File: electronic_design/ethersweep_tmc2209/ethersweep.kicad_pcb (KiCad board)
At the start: 2 copper layers, 79 x 38 mm, 101 parts, among them J1 AVR-ISP-6, J10 HR911105A, J11 Conn_01x04_Male, J2 Conn_01x02_Male, J3 Conn_01x04_Female, J4 Conn_01x02_Male, J5 Conn_01x02_Male, J6 Conn_01x07_Female, J7 Conn_01x07_Male, J8 AVR-ISP-6, J9 USB_B_Micro, SW1 SW_Push, U1 CP2102N-A01-GQFN28, U2 ATmega328-AU, U3 TMC2208-LA-T, U4 DD4012SA, U5 AS5600, U6 W5500, Y2 Crystal_25MHz, Y3 Crystal

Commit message: major commit for ethersweep 4 with STM32 MCU and USB C + fixes
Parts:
- removed C22: C100nF, Capacitor_SMD:C_0805_2012Metric
- removed G***: LOGO, ethernet_motor_driver:CODE Logo
- removed G***: LOGO, Logo:neumann_prototypen_tiny
- removed G***: LOGO, Logo:neumann_prototypen_small
- removed REF**: WEEE-Logo_4.2x6mm_SilkScreen, Symbol:WEEE-Logo_4.2x6mm_SilkScreen
- added C28: C100nF, Capacitor_SMD:C_0402_1005Metric, F.Cu at (252.1, 104.3)
- added C31: C10uF, Capacitor_SMD:C_0402_1005Metric, F.Cu at (212.3, 48.8)
- added J12: USB_C_Receptacle, Connector_USB:USB_C_Receptacle_XKB_U262-16XN-4BVC11, F.Cu at (199.6, 62.6)
- added U7: TMC2209-LA, KiCad:TMC2209-LA, F.Cu at (242.6, 31.8)
- added U8: STUSB4500QTR, Package_CSP:ST_WLCSP-25_Die444, F.Cu at (196.6, 55.6)
- C1, C12, C19, C20, C21, C23, C27, C29, C6: footprint Capacitor_SMD:C_0805_2012Metric -> Capacitor_SMD:C_0402_1005Metric
- C11: value C0.22uF -> C2.2-4.7uF ceramic; footprint Capacitor_SMD:C_0805_2012Metric -> Capacitor_SMD:C_1206_3216Metric
- C13, C35, C7: footprint Capacitor_SMD:C_0603_1608Metric -> Capacitor_SMD:C_0402_1005Metric
- C18: value C22nF -> C100nF; footprint Capacitor_SMD:C_0805_2012Metric -> Capacitor_SMD:C_0402_1005Metric
- C30: footprint Capacitor_SMD:C_0805_2012Metric -> Capacitor_SMD:C_0603_1608Metric
- C9: value C100nF -> C22nF 50V
- J4, J5: value Conn_01x02_Male -> Conn_01x03_Male; footprint Connector_JST:JST_EH_S2B-EH_1x02_P2.50mm_Horizontal -> Connector_JST:JST_EH_S3B-EH_1x03_P2.50mm_Horizontal
- R1, R14, R15, R16, R17, R2, R21, R22, R3: footprint Resistor_SMD:R_0603_1608Metric -> Resistor_SMD:R_0402_1005Metric
- R4, R5, R6, R7, R8: footprint Resistor_SMD:R_0805_2012Metric -> Resistor_SMD:R_0603_1608Metric
- U3: value TMC2208-LA-T -> STM32F103RBTx; footprint Package_DFN_QFN:TQFN-28-1EP_5x5mm_P0.5mm_EP3.25x3.25mm_ThermalVias -> Package_QFP:LQFP-64_10x10mm_P0.5mm
- moved C24 123.5 mm to (255.6, 107.8), turned to 0 degrees
- moved C14 116.4 mm to (275.8, 19.3)
- moved C25 114.3 mm to (256.2, 104.4)
- moved D2 114.3 mm to (302.3, 50.6), turned to 0 degrees
- moved R3 112.2 mm to (281.3, 41.6), turned to 0 degrees
- moved C19 111.9 mm to (314.9, 25.5)
- moved R24 109.1 mm to (298.6, 50.8), turned to 0 degrees
- moved R16 109.0 mm to (310.8, 23.1), turned to 0 degrees
- moved R17 108.3 mm to (311.3, 28.3)
- moved R14 102.0 mm to (285.3, 12.1), turned to 0 degrees
- moved C8 99.0 mm to (288.3, 32.3), turned to 0 degrees
- moved Y3 98.5 mm to (290.1, 25.8), turned to 0 degrees
- moved C10 94.3 mm to (291.2, 32.3), turned to 0 degrees
- moved C29 94.3 mm to (242.3, 41.8), turned to 0 degrees
- moved R15 90.5 mm to (290.6, 12.6), turned to 0 degrees
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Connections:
- C14 pad 1: +3.3VA -> +3V3
- C18 pad 1: Net-(C18-Pad1) -> +3.3VA
- C18 pad 2: Net-(C18-Pad2) -> GND
- C20 pad 1: Net-(C20-Pad1) -> +3.3VA
- C21 pad 1: Net-(C21-Pad1) -> +3.3VA
- C23 pad 2: GND -> Net-(C23-Pad2)
- C24 pad 1: +3.3VA -> GND
- C24 pad 2: GND -> Net-(C24-Pad2)
- C25 pad 1: +3.3VA -> Net-(C25-Pad1)
- C27 pad 1: rst -> +12V
- C27 pad 2: Net-(C27-Pad2) -> GND
- C29 pad 1: +3V3 -> +12V
- C9 pad 2: +12V -> Net-(C9-Pad2)
- J4 pad 2: ESTOP -> +3V3
- J5 pad 2: ENDSTOP -> +3V3
- J9 pad 1: Net-(C21-Pad1) -> Net-(C25-Pad1)
- R1 pad 2: ESTOP -> ENDSTOP
- R11 pad 1: Net-(R11-Pad1) -> GND
- R11 pad 2: GND -> Net-(R11-Pad2)
- R12 pad 1: Net-(R12-Pad1) -> GND
- R12 pad 2: GND -> Net-(R12-Pad2)
- R2 pad 2: ENDSTOP -> ESTOP
- RV1 pad 1: +3V3 -> GND
- RV1 pad 3: GND -> +3V3
- U1 pad 28: Net-(C27-Pad2) -> Net-(C28-Pad2)
- U1 pad 6: Net-(C20-Pad1) -> Net-(C24-Pad2)
- U1 pad 7: Net-(C21-Pad1) -> Net-(C25-Pad1)
- U1 pad 8: Net-(C21-Pad1) -> Net-(C25-Pad1)
- U2 pad 10: DIR -> unconnected-(U2-Pad10)
- U2 pad 11: STEP -> unconnected-(U2-Pad11)
- U2 pad 23: M1 -> unconnected-(U2-Pad23)
- U2 pad 24: M0 -> unconnected-(U2-Pad24)
- U2 pad 25: M2 -> unconnected-(U2-Pad25)
- U2 pad 26: FLT_STEPPER -> unconnected-(U2-Pad26)
- U2 pad 9: STEPPER_ENABLE -> unconnected-(U2-Pad9)
- U3 pad 1: Net-(J11-Pad4) -> unconnected-(U3-Pad1)
- U3 pad 10: M1 -> unconnected-(U3-Pad10)
- U3 pad 11: M2 -> unconnected-(U3-Pad11)
- U3 pad 12: FLT_STEPPER -> unconnected-(U3-Pad12)
- U3 pad 13: GND -> unconnected-(U3-Pad13)
- U3 pad 14: GND -> unconnected-(U3-Pad14)
- U3 pad 15: +3V3 -> unconnected-(U3-Pad15)
- U3 pad 16: STEP -> unconnected-(U3-Pad16)
- U3 pad 17: Net-(RV1-Pad2) -> unconnected-(U3-Pad17)
- U3 pad 18: GND -> unconnected-(U3-Pad18)
- U3 pad 19: DIR -> unconnected-(U3-Pad19)
- U3 pad 2: STEPPER_ENABLE -> unconnected-(U3-Pad2)
- U3 pad 20: GND -> unconnected-(U3-Pad20)
- U3 pad 21: Net-(J11-Pad1) -> unconnected-(U3-Pad21)
- U3 pad 22: +12V -> unconnected-(U3-Pad22)
- U3 pad 23: Net-(R11-Pad1) -> unconnected-(U3-Pad23)
- U3 pad 24: Net-(J11-Pad3) -> unconnected-(U3-Pad24)
- U3 pad 25: GND -> unconnected-(U3-Pad25)
- U3 pad 26: Net-(J11-Pad2) -> unconnected-(U3-Pad26)
- U3 pad 27: Net-(R12-Pad1) -> unconnected-(U3-Pad27)
- U3 pad 28: +12V -> unconnected-(U3-Pad28)
- U3 pad 29: GND -> unconnected-(U3-Pad29)
- U3 pad 3: GND -> unconnected-(U3-Pad3)
- U3 pad 4: Net-(C18-Pad1) -> unconnected-(U3-Pad4)
- U3 pad 5: Net-(C18-Pad2) -> unconnected-(U3-Pad5)
- U3 pad 6: Net-(C9-Pad1) -> unconnected-(U3-Pad6)
- U3 pad 7: GND -> unconnected-(U3-Pad7)
- U3 pad 8: Net-(C11-Pad1) -> unconnected-(U3-Pad8)
- U3 pad 9: M0 -> unconnected-(U3-Pad9)
- U6 pad 32: CS_ETHERNET -> GND
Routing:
- net +3V3: track 201.4 -> 117.3 mm, vias 10 -> 3
- net +12V: track 70.3 -> 0.00 mm, vias 6 -> 0
- net rst: track 62.0 -> 6.23 mm, vias 1 -> 0
- net STEPPER_ENABLE: track 40.4 -> 0.00 mm, vias 2 -> 0
- net FLT_STEPPER: track 38.2 -> 0.00 mm, vias 2 -> 0
- net GND: track 73.4 -> 36.4 mm, vias 226 -> 105
- net M2: track 36.2 -> 0.00 mm, vias 2 -> 0
- net SDA: track 115.7 -> 80.1 mm, vias 3 -> 0
- net M0: track 34.5 -> 0.00 mm, vias 2 -> 0
- net DIR: track 34.5 -> 0.00 mm, vias 2 -> 0
- net STEP: track 33.6 -> 0.00 mm, vias 2 -> 0
- net M1: track 32.9 -> 0.00 mm, vias 2 -> 0
- net uC_RX: track 31.2 -> 0.00 mm, vias 3 -> 0
- net SCL: track 109.9 -> 79.0 mm, vias 1 -> 0
- net ESTOP: track 68.9 -> 40.1 mm, vias 1 -> 0
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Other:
- board text added: "2023-01-10"
- board text added: "rev. 4.0.1"
- board text removed: "2022-10-05"
- board text removed: "3.3V"
- board text removed: "GND"
- board text removed: "RX"
- board text removed: "TX"
- board text removed: "rev. 3.0.5"

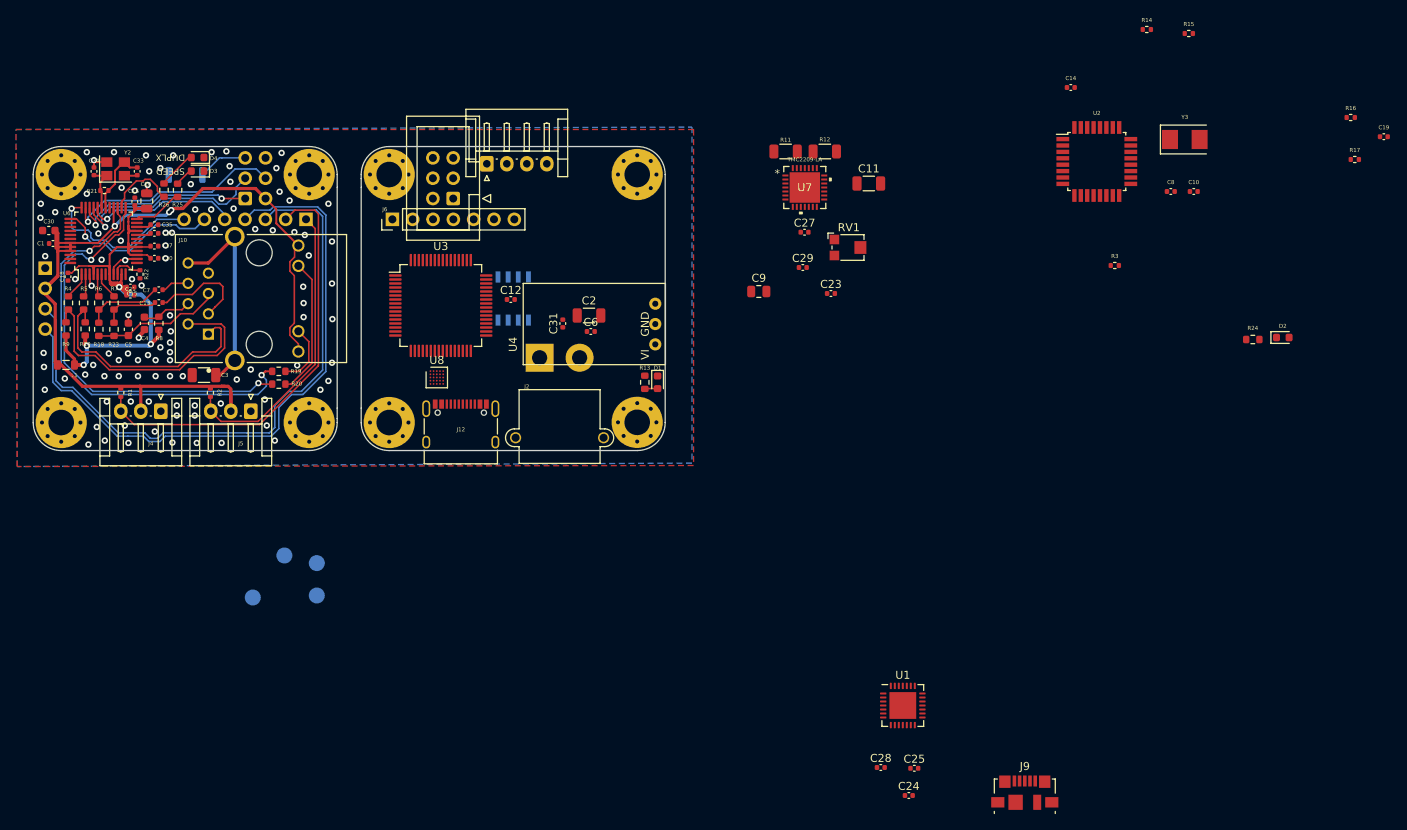
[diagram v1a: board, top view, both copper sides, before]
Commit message: cleanup, schmeatic design around USB connecotr, STM32 and reorganisation
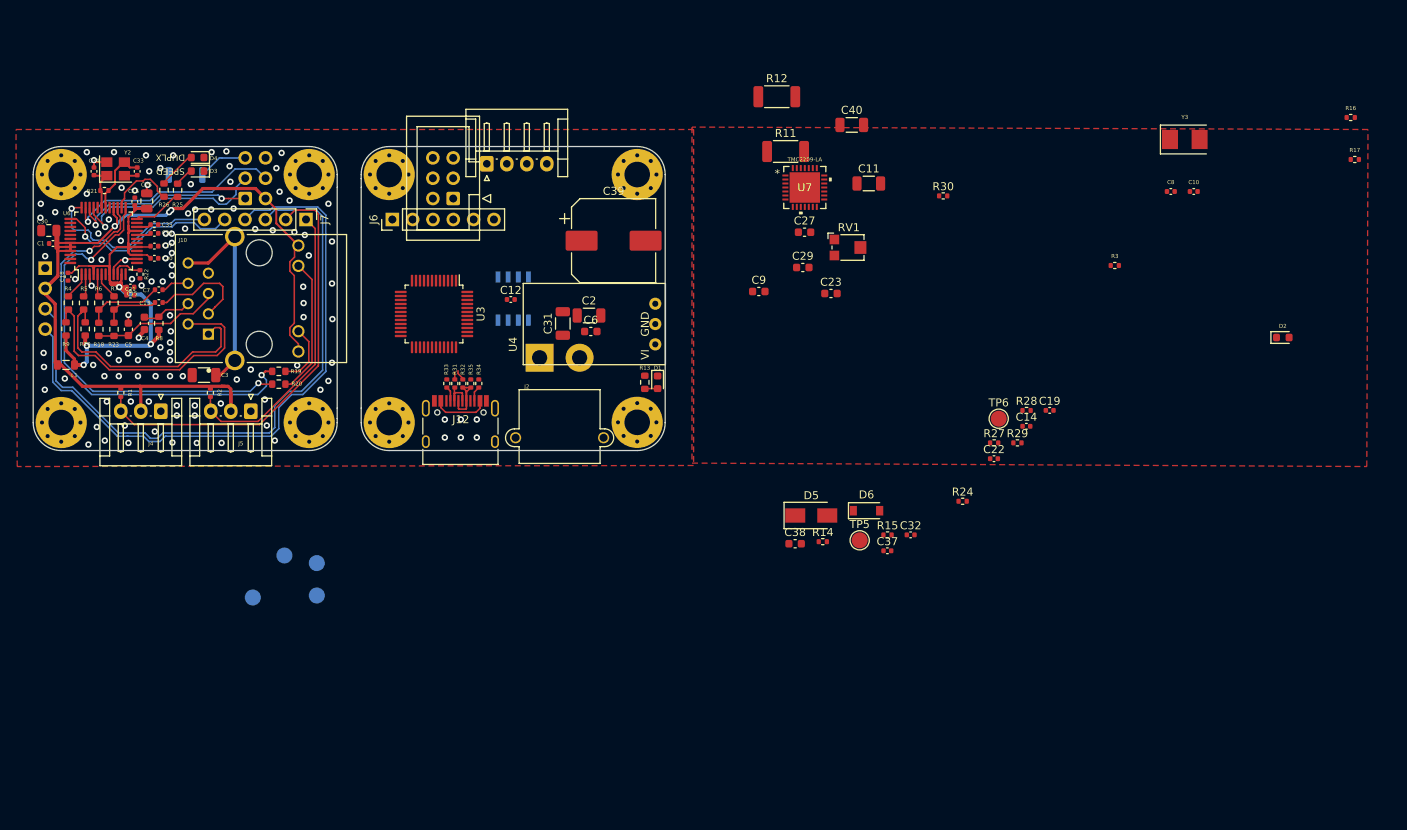
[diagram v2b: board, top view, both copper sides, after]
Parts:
- removed C24, C25, C28: C100nF, Capacitor_SMD:C_0402_1005Metric
- removed J9: USB_B_Micro, Connector_USB:USB_Micro-B_Molex_47346-0001
- removed U1: CP2102N-A01-GQFN28, Package_DFN_QFN:QFN-28-1EP_5x5mm_P0.5mm_EP3.35x3.35mm
- removed U2: ATmega328-AU, Package_QFP:TQFP-32_7x7mm_P0.8mm
- removed U8: STUSB4500QTR, Package_CSP:ST_WLCSP-25_Die444
- added C22: C100nF, Capacitor_SMD:C_0402_1005Metric, F.Cu at (266.2, 65.7)
- added C32: C100nF, Capacitor_SMD:C_0402_1005Metric, F.Cu at (255.8, 75.2)
- added C37: C100nF, Capacitor_SMD:C_0402_1005Metric, F.Cu at (252.9, 77.2)
- added C38: C100nF, Capacitor_SMD:C_0603_1608Metric, F.Cu at (241.3, 76.3)
- added C39: C_330uF, Capacitor_SMD:CP_Elec_10x10, F.Cu at (218.7, 38.5)
- added C40: C10uF, Capacitor_SMD:C_1206_3216Metric, F.Cu at (248.4, 24.0)
- added D5: D_TVS_5V, Diode_SMD:D_SMA, F.Cu at (243.4, 72.8)
- added D6: D_TVS_30V, Diode_SMD:D_SOD-123, F.Cu at (250.3, 72.2)
- added R27: R10k, Resistor_SMD:R_0402_1005Metric, F.Cu at (266.2, 63.7)
- added R28: R10k, Resistor_SMD:R_0402_1005Metric, F.Cu at (270.3, 59.7)
- added R29: R10k, Resistor_SMD:R_0402_1005Metric, F.Cu at (269.1, 63.7)
- added R30: R1k, Resistor_SMD:R_0402_1005Metric, F.Cu at (259.9, 32.9)
- added R31: R22, Resistor_SMD:R_0402_1005Metric, F.Cu at (198.8, 56.3)
- added R32: R22, Resistor_SMD:R_0402_1005Metric, F.Cu at (199.8, 56.3)
- added R33: R5.1k, Resistor_SMD:R_0402_1005Metric, F.Cu at (197.8, 56.3)
- added R34: R5.1k, Resistor_SMD:R_0402_1005Metric, F.Cu at (201.8, 56.3)
- added R35: R1.5k, Resistor_SMD:R_0402_1005Metric, F.Cu at (200.8, 56.3)
- added TP5: BOOT_1, TestPoint:TestPoint_Pad_D2.0mm, F.Cu at (249.4, 75.9)
- added TP6: BOOT_0, TestPoint:TestPoint_Pad_D2.0mm, F.Cu at (266.8, 60.7)
- C23, C27, C29, C6: footprint Capacitor_SMD:C_0402_1005Metric -> Capacitor_SMD:C_0603_1608Metric
- C30: footprint Capacitor_SMD:C_0603_1608Metric -> Capacitor_SMD:C_0805_2012Metric
- C31: footprint Capacitor_SMD:C_0402_1005Metric -> Capacitor_SMD:C_1206_3216Metric
- C9: footprint Capacitor_SMD:C_0805_2012Metric -> Capacitor_SMD:C_0603_1608Metric
- J12: value USB_C_Receptacle -> USB_C_Receptacle_USB2.0; footprint Connector_USB:USB_C_Receptacle_XKB_U262-16XN-4BVC11 -> Connector_USB:USB_C_Receptacle_HRO_TYPE-C-31-M-12
- J6: value Conn_01x07_Female -> Conn_01x06_Female; footprint Connector_PinHeader_2.54mm:PinHeader_1x07_P2.54mm_Vertical -> Connector_PinHeader_2.54mm:PinHeader_1x06_P2.54mm_Vertical
- J7: value Conn_01x07_Male -> Conn_01x06_Male; footprint Connector_PinHeader_2.54mm:PinHeader_1x07_P2.54mm_Vertical -> Connector_PinHeader_2.54mm:PinHeader_1x06_P2.54mm_Vertical; moved to F.Cu
- R11, R12: value R180mOHM -> R100mOHM; footprint Resistor_SMD:R_1206_3216Metric -> Resistor_SMD:R_2010_5025Metric
- R14: value R1k -> R1M
- R24: value R330 -> R10k; footprint Resistor_SMD:R_0603_1608Metric -> Resistor_SMD:R_0402_1005Metric
- TP1: value TestPoint -> 3.3V
- TP2: value TestPoint -> GND
- TP3: value TestPoint -> RX
- TP4: value TestPoint -> TX
- U3: value STM32F103RBTx -> STM32F103C8Tx; footprint Package_QFP:LQFP-64_10x10mm_P0.5mm -> Package_QFP:LQFP-48_7x7mm_P0.5mm
- moved R14 75.8 mm to (244.8, 76.1)
- moved R15 73.1 mm to (252.9, 75.2)
- moved C19 54.0 mm to (273.2, 59.7)
- moved C14 42.7 mm to (270.2, 61.7)
- moved R24 41.5 mm to (262.3, 71.0)
- moved R12 9.11 mm to (239.1, 20.5)
- moved U3 1.36 mm to (196.2, 47.6), turned to -90 degrees
- moved J12 0.06 mm to (199.5, 62.5)
- turned J7 to -90 degrees
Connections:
- net +12V renamed +28V
- C19 pad 1: voltage_detect -> +3V3
- J12 pad A1: Net-(J12-PadA1) -> GND
- J12 pad A12: Net-(J12-PadA1) -> GND
- J12 pad A5: unconnected-(J12-PadA5) -> Net-(J12-PadA5)
- J12 pad A6: unconnected-(J12-PadA6) -> Net-(J12-PadA6)
- J12 pad A7: unconnected-(J12-PadA7) -> Net-(J12-PadA7)
- J12 pad B1: Net-(J12-PadA1) -> GND
- J12 pad B12: Net-(J12-PadA1) -> GND
- J12 pad B5: unconnected-(J12-PadB5) -> Net-(J12-PadB5)
- J12 pad B6: unconnected-(J12-PadB6) -> Net-(J12-PadA6)
- J12 pad B7: unconnected-(J12-PadB7) -> Net-(J12-PadA7)
- J12 pad S1: unconnected-(J12-PadS1) -> GND
- J6 pad 5: CS_ETHERNET -> RST_ETHERNET
- J6 pad 6: RST_ETHERNET -> ETH_INT
- J7 pad 5: CS_ETHERNET -> RST_ETHERNET
- J7 pad 6: RST_ETHERNET -> ETH_INT
- R14 pad 1: +3V3 -> Net-(C10-Pad2)
- R14 pad 2: SCL -> Net-(C8-Pad1)
- R15 pad 1: +3V3 -> Net-(D2-Pad2)
- R15 pad 2: SDA -> Net-(R15-Pad2)
- R24 pad 1: Net-(R24-Pad1) -> +3V3
- R24 pad 2: Net-(D2-Pad2) -> SCL
- RV1 pad 2: Net-(RV1-Pad2) -> MOT_VREF_POT
- U3 pad 11: unconnected-(U3-Pad11) -> voltage_detect
- U3 pad 12: unconnected-(U3-Pad12) -> MOT_VREF_POT
- U3 pad 15: unconnected-(U3-Pad15) -> SCK
- U3 pad 16: unconnected-(U3-Pad16) -> MISO
- U3 pad 17: unconnected-(U3-Pad17) -> MOSI
- U3 pad 2: unconnected-(U3-Pad2) -> Net-(R15-Pad2)
- U3 pad 20: unconnected-(U3-Pad20) -> BOOT_1
- U3 pad 23: unconnected-(U3-Pad23) -> GND
- U3 pad 24: unconnected-(U3-Pad24) -> +3V3
- U3 pad 30: unconnected-(U3-Pad30) -> uC_TX
- U3 pad 31: unconnected-(U3-Pad31) -> uC_RX
- U3 pad 32: unconnected-(U3-Pad32) -> USB-
- U3 pad 33: unconnected-(U3-Pad33) -> USB+
- U3 pad 35: unconnected-(U3-Pad35) -> GND
- U3 pad 36: unconnected-(U3-Pad36) -> +3V3
- U3 pad 42: unconnected-(U3-Pad42) -> SCL
- U3 pad 43: unconnected-(U3-Pad43) -> SDA
- U3 pad 44: unconnected-(U3-Pad44) -> BOOT_0
- U3 pad 47: unconnected-(U3-Pad47) -> GND
- U3 pad 48: unconnected-(U3-Pad48) -> +3V3
- U3 pad 5: unconnected-(U3-Pad5) -> Net-(C10-Pad2)
- U3 pad 6: unconnected-(U3-Pad6) -> Net-(C8-Pad1)
- U3 pad 7: unconnected-(U3-Pad7) -> rst
- U3 pad 8: unconnected-(U3-Pad8) -> GND
- U3 pad 9: unconnected-(U3-Pad9) -> +3V3
- U7 pad 13: MOT_CLK -> GND
- U7 pad 14: MOT_UART_PDN -> MOT_UART_RX
- U7 pad 17: Net-(RV1-Pad2) -> MOT_VREF_POT
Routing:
- net GND: track 36.4 -> 17.2 mm, vias 105 -> 117
- net Net-(J12-PadA6): track 0.00 -> 7.74 mm
- net Net-(J12-PadA4): track 0.00 -> 7.11 mm
- net Net-(J12-PadA7): track 0.00 -> 4.68 mm
- net RST_ETHERNET: track 21.5 -> 24.8 mm
- net ETH_INT: track 20.6 -> 23.6 mm
- net Net-(J12-PadB5): track 0.00 -> 1.89 mm
- net Net-(J12-PadA5): track 0.00 -> 1.85 mm
- net USB+: track 0.00 -> 1.34 mm
- net USB-: track 0.00 -> 0.92 mm
- removed copper zone on B.Cu, net GND

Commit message: layout version 4 in manufacturable state: STM32, TMC2209, USBC, 3 pin switches
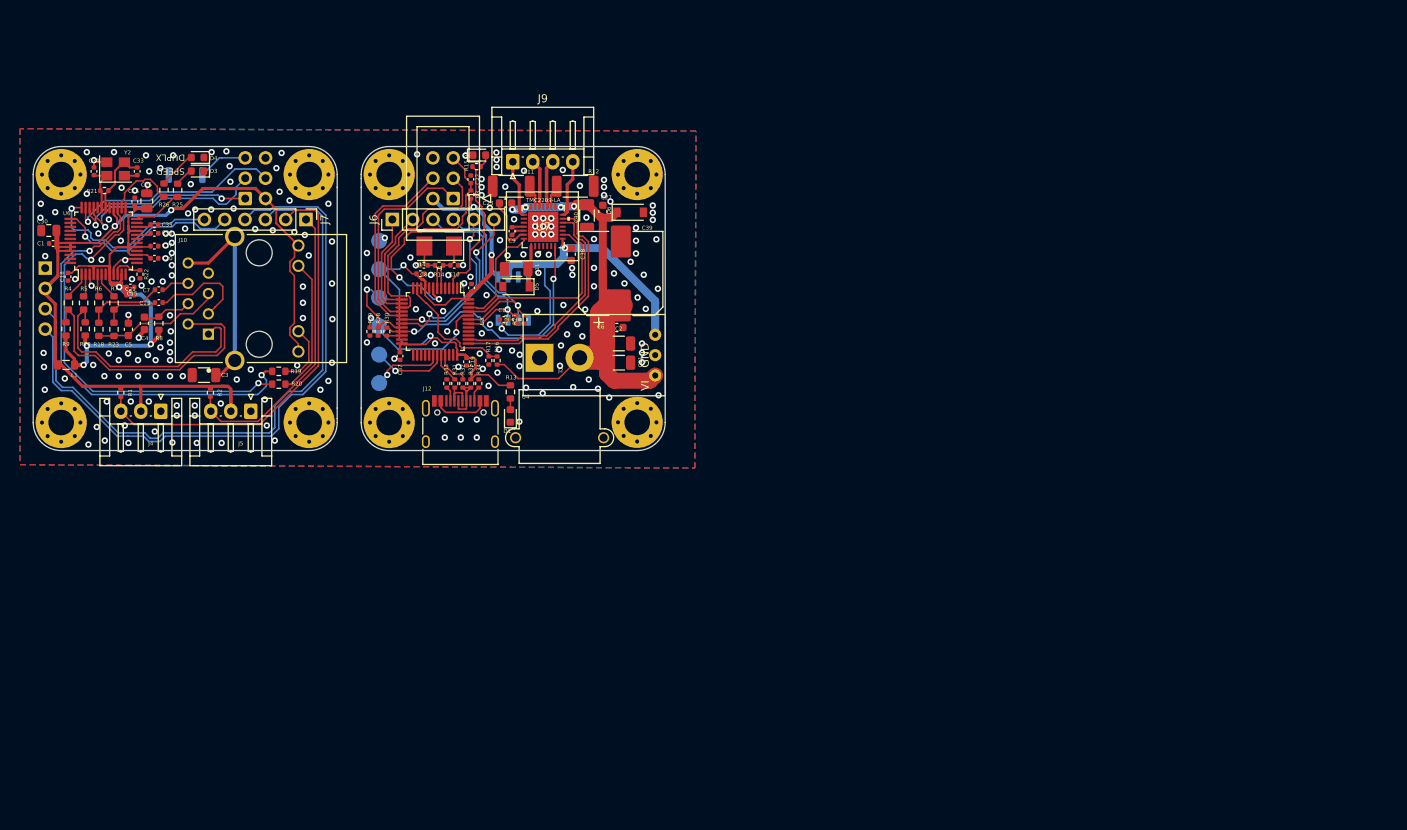
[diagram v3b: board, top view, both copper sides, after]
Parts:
- removed C29: C100nF, Capacitor_SMD:C_0603_1608Metric
- removed J11: Conn_01x04_Male, Connector_JST:JST_EH_S4B-EH_1x04_P2.50mm_Horizontal
- removed RV1: R_POT_20K, Potentiometer_SMD:Potentiometer_Bourns_TC33X_Vertical
- added J9: Conn_01x04_Female, Connector_JST:JST_EH_S4B-EH_1x04_P2.50mm_Horizontal, F.Cu at (206.1, 28.6)
- C9: footprint Capacitor_SMD:C_0603_1608Metric -> Capacitor_SMD:C_0402_1005Metric
- D5: footprint Diode_SMD:D_SMA -> Diode_SMD:D_SOD-123
- TP5, TP6: moved to B.Cu
- moved R17 111.1 mm to (203.1, 53.4), turned to -90 degrees
- moved R16 110.9 mm to (204.1, 53.5), turned to 90 degrees
- moved D2 103.0 mm to (201.9, 27.8)
- moved Y3 94.1 mm to (196.8, 39.1), turned to 180 degrees
- moved C8 93.8 mm to (194.9, 41.5), turned to 180 degrees
- moved C10 92.9 mm to (198.7, 41.5), turned to 180 degrees
- moved R29 82.1 mm to (188.2, 49.8), turned to 90 degrees
- moved R28 81.6 mm to (189.2, 49.8), turned to 90 degrees
- moved R3 81.0 mm to (200.8, 32.7), turned to 90 degrees
- moved TP6 78.3 mm to (189.3, 49.2), turned to 180 degrees
- moved C14 78.1 mm to (194.5, 42.6)
- moved C22 74.1 mm to (200.8, 30.8), turned to -90 degrees
- moved C19 73.1 mm to (200.3, 53.6), turned to -90 degrees
- moved R30 71.6 mm to (190.3, 49.8), turned to 90 degrees
- moved R15 69.0 mm to (201.5, 29.2), turned to 180 degrees
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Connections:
- U3 pad 12: MOT_VREF_POT -> unconnected-(U3-Pad12)
- U3 pad 13: unconnected-(U3-Pad13) -> ENDSTOP
- U3 pad 14: unconnected-(U3-Pad14) -> ESTOP
- U3 pad 18: unconnected-(U3-Pad18) -> ETH_INT
- U3 pad 19: unconnected-(U3-Pad19) -> RST_ETHERNET
- U3 pad 21: unconnected-(U3-Pad21) -> MOT_UART_RX
- U3 pad 22: unconnected-(U3-Pad22) -> MOT_UART_TX
- U3 pad 37: unconnected-(U3-Pad37) -> MOT_STANDBY
- U3 pad 38: unconnected-(U3-Pad38) -> MOT_DIR
- U3 pad 45: unconnected-(U3-Pad45) -> MOT_STEP
- U3 pad 46: unconnected-(U3-Pad46) -> MOT_SPREAD
- U7 pad 17: MOT_VREF_POT -> unconnected-(U7-Pad17)
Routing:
- net +3V3: track 117.5 -> 248.8 mm, vias 3 -> 8
- net +28V: track 0.00 -> 78.4 mm, vias 0 -> 4
- net MOT_UART_RX: track 0.00 -> 35.6 mm, vias 0 -> 2
- net rst: track 6.23 -> 38.6 mm, vias 0 -> 2
- net MOT_STANDBY: track 0.00 -> 29.7 mm
- net MOT_DIR: track 0.00 -> 28.3 mm
- net SCK: track 25.9 -> 53.3 mm
- net SDA: track 80.1 -> 106.7 mm, vias 0 -> 1
- net SCL: track 79.0 -> 105.3 mm, vias 0 -> 1
- net MISO: track 23.5 -> 48.8 mm
- net MOT_STEP: track 0.00 -> 24.2 mm
- net MOSI: track 28.2 -> 52.2 mm
- net ETH_INT: track 23.6 -> 45.0 mm, vias 1 -> 3
- net RST_ETHERNET: track 24.8 -> 46.1 mm, vias 1 -> 3
- net Net-(R15-Pad2): track 0.00 -> 18.4 mm
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- added copper zone on B.Cu, net GND
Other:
- board text added: "ETHERSWEEP 2023-01-10"
- board text removed: "2023-01-10"
